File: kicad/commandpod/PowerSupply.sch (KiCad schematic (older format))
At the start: 10 parts

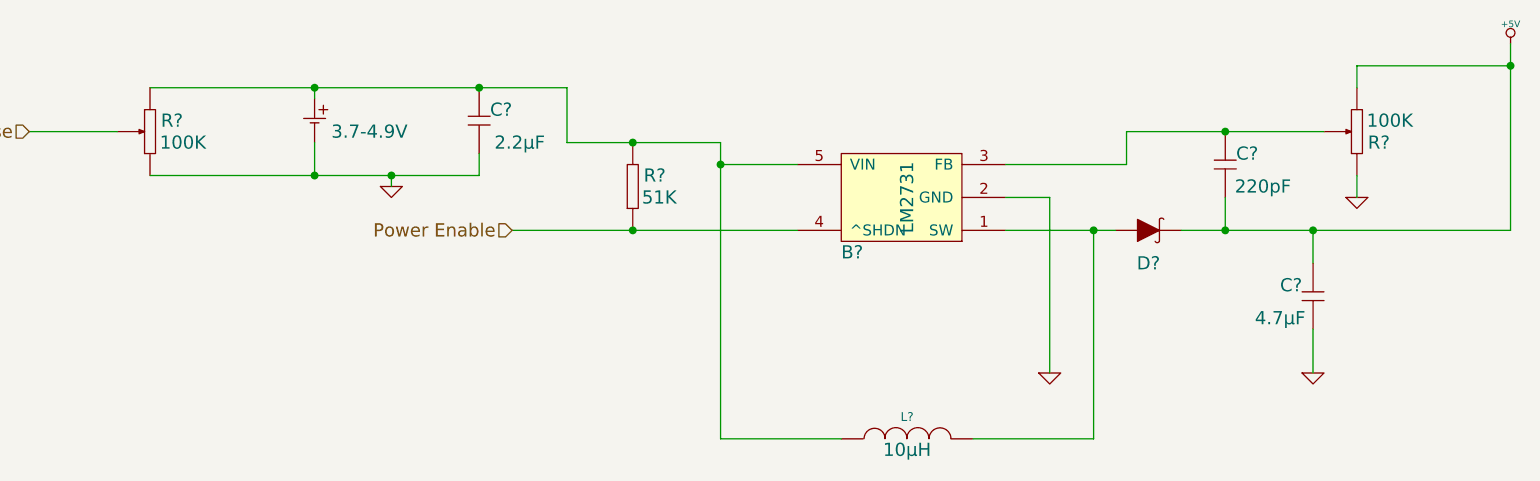
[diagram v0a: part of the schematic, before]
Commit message: Annotated schematics
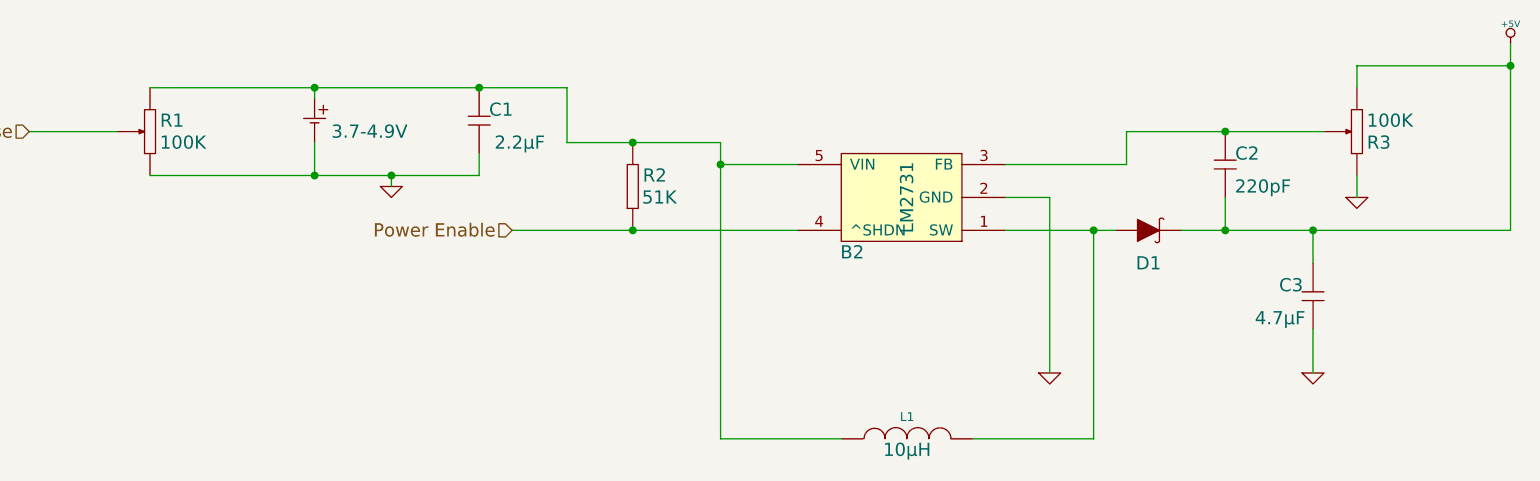
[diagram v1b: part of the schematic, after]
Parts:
- gave numbers to parts that had none: 10
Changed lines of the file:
@@
 $EndDescr
 $Comp
-L LM2731 B?
+L LM2731 B2
 U 1 1 56D7A438
 P 6000 4100
-F 0 "B?" H 6200 4350 60  0000 C CNN
+F 0 "B2" H 6200 4350 60  0000 C CNN
 F 1 "LM2731" V 5950 4100 60  0000 C CNN
 F 2 "~" H 5900 4100 60  0000 C CNN
@@
 $EndComp
 $Comp
-L GENERIC_RESISTOR R?
+L GENERIC_RESISTOR R2
 U 1 1 56D7A440
 P 4800 4050
-F 0 "R?" V 4850 3950 60  0000 C CNN
+F 0 "R2" V 4850 3950 60  0000 C CNN
 F 1 "GENERIC_RESISTOR" H 4840 3830 60  0001 C CNN
 F 2 "~" H 4750 3800 60  0000 C CNN
@@
 $EndComp
 $Comp
-L BATTERY_ B?
+L BATTERY_ B1
 U 1 1 56D7A447
 P 3350 3750
-F 0 "B?" V 3300 3900 60  0001 C CNN
+F 0 "B1" V 3300 3900 60  0001 C CNN
 F 1 "BATTERY_" H 3350 3950 60  0001 C CNN
 F 2 "" H 3350 3750 60  0000 C CNN
@@
 $EndComp
 $Comp
-L GENERIC_CAPACITOR C?
+L GENERIC_CAPACITOR C1
 U 1 1 56D7A44F
 P 4100 3750
-F 0 "C?" V 4150 3650 60  0000 C CNN
+F 0 "C1" V 4150 3650 60  0000 C CNN
 F 1 "GENERIC_CAPACITOR" H 4110 3550 60  0001 C CNN
 F 2 "~" H 4070 3500 60  0000 C CNN
@@
 $EndComp
 $Comp
-L GND #PWR?
+L GND #PWR05
 U 1 1 56D7A455
 P 6700 4900
-F 0 "#PWR?" H 6700 4900 30  0001 C CNN
+F 0 "#PWR05" H 6700 4900 30  0001 C CNN
 F 1 "GND" H 6700 4830 30  0001 C CNN
 F 2 "" H 6700 4900 60  0000 C CNN
@@
 $EndComp
 $Comp
-L SCHOTTKY_DIODE D?
+L SCHOTTKY_DIODE D1
 U 1 1 56D7A45C
 P 7150 4250
-F 0 "D?" H 7150 4100 60  0000 C CNN
+F 0 "D1" H 7150 4100 60  0000 C CNN
 F 1 "SCHOTTKY_DIODE" H 7150 4400 60  0001 C CNN
 F 2 "~" H 7150 4250 60  0000 C CNN
@@
 $EndComp
 $Comp
-L +5V #PWR?
+L +5V #PWR06
 U 1 1 56D7A462
 P 8800 3400
-F 0 "#PWR?" H 8800 3490 20  0001 C CNN
+F 0 "#PWR06" H 8800 3490 20  0001 C CNN
 F 1 "+5V" H 8800 3490 30  0000 C CNN
 F 2 "" H 8800 3400 60  0000 C CNN
@@
 $EndComp
 $Comp
-L INDUCTOR L?
+L INDUCTOR L1
 U 1 1 56D7A469
 P 6050 5200
-F 0 "L?" V 6150 5200 40  0000 C CNN
+F 0 "L1" V 6150 5200 40  0000 C CNN
 F 1 "INDUCTOR" V 6150 5200 40  0001 C CNN
 F 2 "~" H 6050 5200 60  0000 C CNN
@@
 $EndComp
 $Comp
-L VARIABLE_RESISTOR R?
+L VARIABLE_RESISTOR R3
 U 1 1 56D7A471
 P 8100 3800
-F 0 "R?" V 8050 3700 60  0000 C CNN
+F 0 "R3" V 8050 3700 60  0000 C CNN
 F 1 "VARIABLE_RESISTOR" H 8140 3580 60  0001 C CNN
 F 2 "~" H 8050 3550 60  0000 C CNN
@@
 $EndComp
 $Comp
-L GND #PWR?
+L GND #PWR07
 U 1 1 56D7A477
 P 7900 4900
-F 0 "#PWR?" H 7900 4900 30  0001 C CNN
+F 0 "#PWR07" H 7900 4900 30  0001 C CNN
 F 1 "GND" H 7900 4830 30  0001 C CNN
 F 2 "" H 7900 4900 60  0000 C CNN
@@
 $EndComp
 $Comp
-L GENERIC_CAPACITOR C?
+L GENERIC_CAPACITOR C3
 U 1 1 56D7A47F
 P 7900 4550
-F 0 "C?" V 7950 4650 60  0000 C CNN
+F 0 "C3" V 7950 4650 60  0000 C CNN
 F 1 "GENERIC_CAPACITOR" H 7910 4350 60  0001 C CNN
 F 2 "~" H 7870 4300 60  0000 C CNN
@@
 $EndComp
 $Comp
-L GENERIC_CAPACITOR C?
+L GENERIC_CAPACITOR C2
 U 1 1 56D7A487
 P 7500 3950
-F 0 "C?" V 7550 3850 60  0000 C CNN
+F 0 "C2" V 7550 3850 60  0000 C CNN
 F 1 "GENERIC_CAPACITOR" H 7510 3750 60  0001 C CNN
 F 2 "~" H 7470 3700 60  0000 C CNN
@@
 Connection ~ 7500 4250
 $Comp
-L GND #PWR?
+L GND #PWR08
 U 1 1 56D7B34B
 P 8100 4100
-F 0 "#PWR?" H 8100 4100 30  0001 C CNN
+F 0 "#PWR08" H 8100 4100 30  0001 C CNN
 F 1 "GND" H 8100 4030 30  0001 C CNN
 F 2 "" H 8100 4100 60  0000 C CNN
@@
 Connection ~ 4800 3850
 $Comp
-L GND #PWR?
+L GND #PWR09
 U 1 1 56D7B7CF
 P 3700 4050
-F 0 "#PWR?" H 3700 4050 30  0001 C CNN
+F 0 "#PWR09" H 3700 4050 30  0001 C CNN
 F 1 "GND" H 3700 3980 30  0001 C CNN
 F 2 "" H 3700 4050 60  0000 C CNN
@@
 Connection ~ 5200 3950
 $Comp
-L VARIABLE_RESISTOR R?
+L VARIABLE_RESISTOR R1
 U 1 1 56D7B88F
 P 2600 3800
-F 0 "R?" V 2650 3700 60  0000 C CNN
+F 0 "R1" V 2650 3700 60  0000 C CNN
 F 1 "VARIABLE_RESISTOR" H 2640 3580 60  0001 C CNN
 F 2 "~" H 2550 3550 60  0000 C CNN

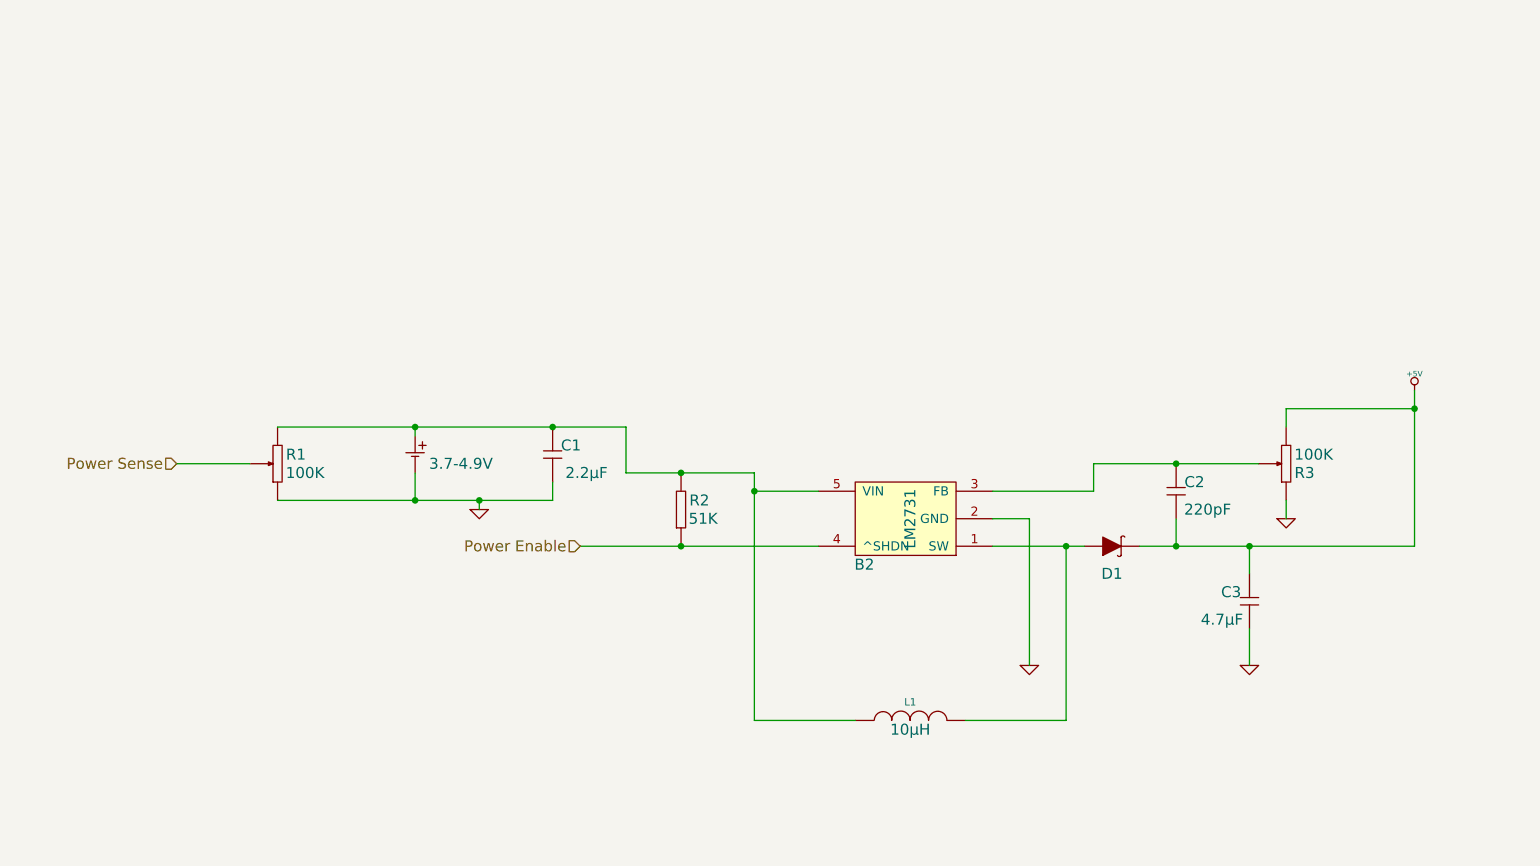
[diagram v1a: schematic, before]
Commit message: Put in charging circuit
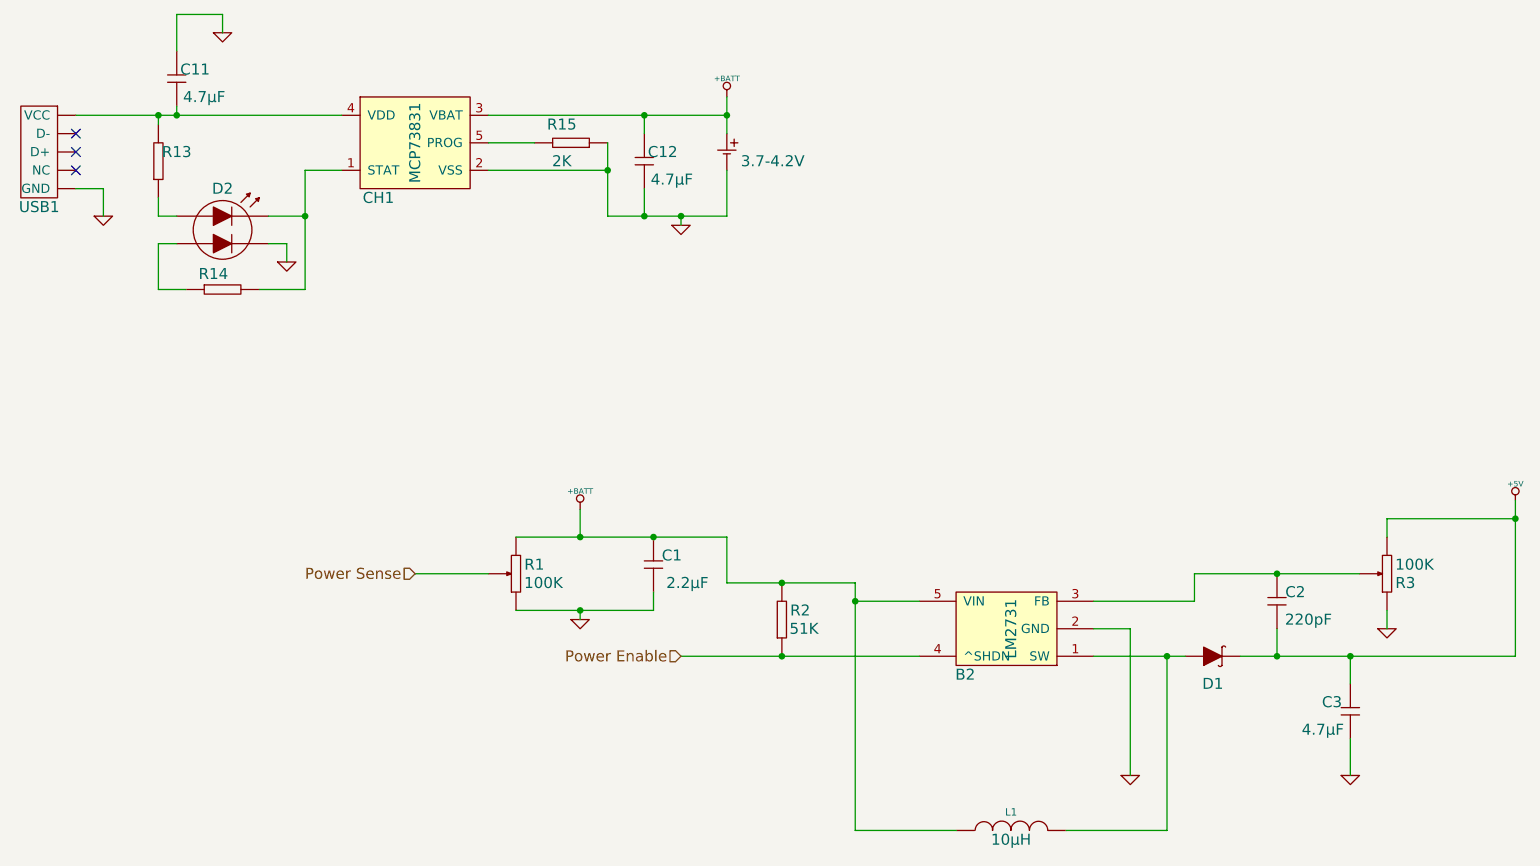
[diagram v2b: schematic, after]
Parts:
- added C11, C12: GENERIC_CAPACITOR, ~, symbol GENERIC_CAPACITOR
- added CH1: MCP73831, symbol MCP73831
- added D2: BICOLOUR_LED, ~, symbol BICOLOUR_LED
- added R13, R14, R15: GENERIC_RESISTOR, ~, symbol GENERIC_RESISTOR
- added USB1: MICRO_USB, symbol MICRO_USB
- B1: Voltage 3.7-4.9V -> 3.7-4.2V
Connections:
- net GND: now also C11.1, C12.2, CH1.2 (VSS), D2.4, R15.2, USB1.5 (GND)
- net +BATT: now reaches B1.1, B2.5 (VIN), C1.1, L1.1, R1.1, R2.1
- net +BATT: now also C12.1, CH1.3 (VBAT)
- new net: CH1.1 (STAT), D2.2, R14.1
- new net: C11.2, CH1.4 (VDD), R13.1, USB1.1 (VCC)
- new net: CH1.5 (PROG), R15.1
- new net: D2.1, R13.2
- new net: D2.3, R14.2
- no-connect marks 0 -> 3
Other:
- moved on the sheet: B2, C1, C2, C3, D1, L1, R1, R2, R3
